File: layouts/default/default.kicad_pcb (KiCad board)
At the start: 2 copper layers, 240 x 47 mm, 129 parts

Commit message: PCB: fix power input orientation and add legends
Route both power cables through the left edge and add durable front and back electrical labels so the assembled dock is unambiguous to power and use.
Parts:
- turned USB1 to 270 degrees
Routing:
- net vdd_cap-power-anode: track 76.1 -> 38.4 mm, vias 10 -> 6
- net DM: track 49.5 -> 15.7 mm, vias 6 -> 0
- net CC2: track 15.5 -> 28.4 mm
- net DP: track 21.5 -> 12.0 mm
- net PG: track 21.2 -> 15.5 mm
- net 9: track 14.2 -> 10.3 mm
- net CC1: track 15.9 -> 16.7 mm, vias 2 -> 0
- net cathode: track 4.63 -> 3.91 mm
- net VBUS: vias 2 -> 0
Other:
- board text added: "12V DC / 5A / CENTER +"
- board text added: "5V OUT / 1A CONT EACH"
- board text added: "INPUT: USB-C PD 12V 36W MAX OR 12V DC 5A CENTER +"
- board text added: "LEDS: RED=PWR BLUE=PD GREEN=CHARGING"
- board text added: "LIGHTBAR DOCK // 8-PORT USB-C CHARGER"
- board text added: "OUTPUT: 5V 1A CONT / PORT (1.5A FUSED)"
- board text added: "PD IN 12V / 36W MAX"
- board text added: "SKG // LIGHTBAR DOCK"
- board text added: "SKG // REV B // 2026"

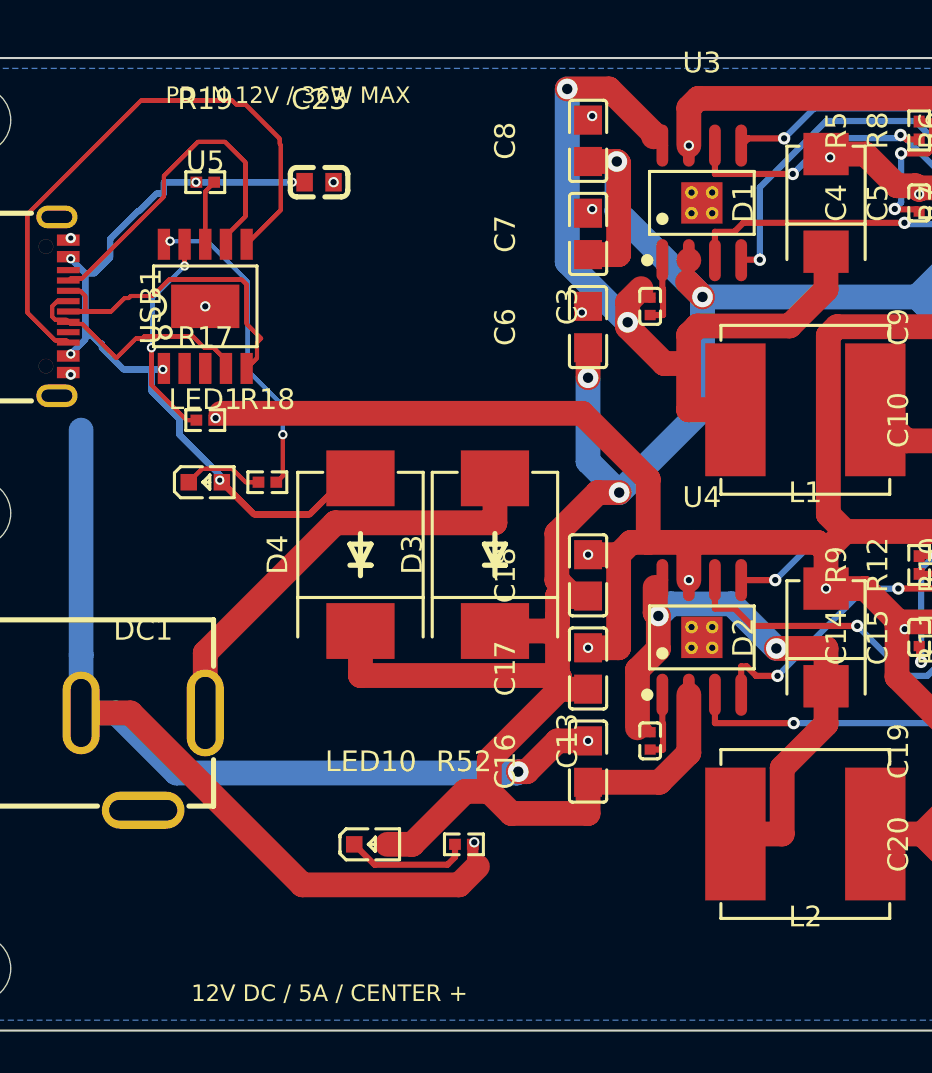
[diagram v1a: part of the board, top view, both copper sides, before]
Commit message: PCB: refresh fabrication outputs and enclosure models
Keep manufacturing and mechanical exports aligned with the corrected power-input geometry and current silkscreen.
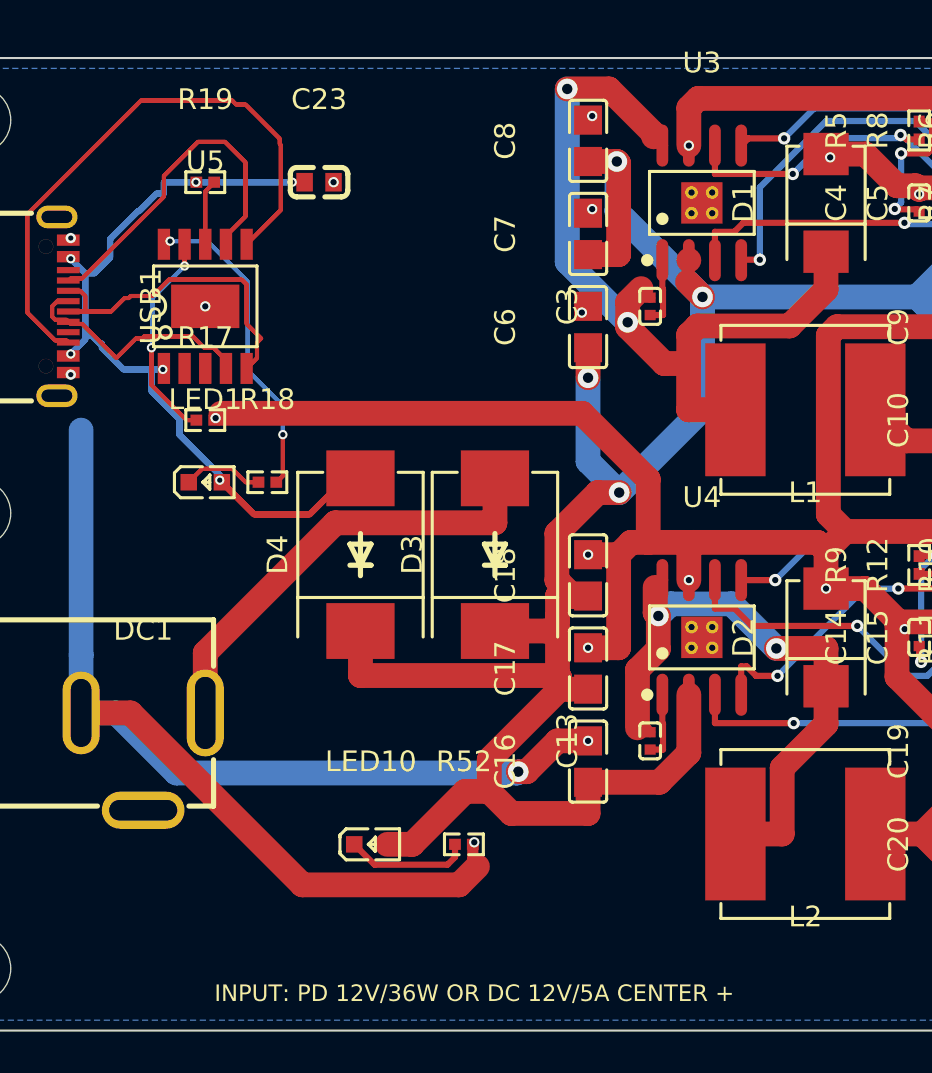
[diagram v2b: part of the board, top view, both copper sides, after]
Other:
- board text added: "INPUT: PD 12V/36W OR DC 12V/5A CENTER +"
- board text removed: "12V DC / 5A / CENTER +"
- board text removed: "PD IN 12V / 36W MAX"
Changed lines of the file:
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@@
 	(footprint "SHOU_HAN_TYPE_C_16PIN_2MD_073:USB-C-SMD_TYPE-C-16PIN-2MD-073"
 		(layer "F.Cu")
-		(at 55 62 270)
+		(at 55 62 -90)
 		(property "Reference" "USB1"
 			(at 0 -6.38 270)
@@
 			)
 			(rotate
-				(xyz 0 0 180)
+				(xyz 0 0 0)
 			)
 		)
@@
 		)
 	)
+	(gr_line
+		(start 50 50)
+		(end 290 50)
+		(stroke
+			(width 0.1)
+			(type default)
+		)
+		(layer "Edge.Cuts")
+	)
+	(gr_line
+		(start 50 97)
+		(end 50 50)
+		(stroke
+			(width 0.1)
+			(type default)
+		)
+		(layer "Edge.Cuts")
+	)
+	(gr_line
+		(start 290 50)
+		(end 290 97)
+		(stroke
+			(width 0.1)
+			(type default)
+		)
+		(layer "Edge.Cuts")
+	)
+	(gr_line
+		(start 290 97)
+		(end 50 97)
+		(stroke
+			(width 0.1)
+			(type default)
+		)
+		(layer "Edge.Cuts")
+	)
+	(gr_text "INPUT: PD 12V/36W OR DC 12V/5A CENTER +"
+		(at 77 95.2 0)
+		(layer "F.SilkS")
+		(effects
+			(font
+				(size 0.8 0.8)
+				(thickness 0.13)
+			)
+		)
+	)
+	(gr_text "5V OUT / 1A CONT EACH"
+		(at 232 95.2 0)
+		(layer "F.SilkS")
+		(effects
+			(font
+				(size 0.8 0.8)
+				(thickness 0.13)
+			)
+		)
+	)
+	(gr_text "SKG // LIGHTBAR DOCK"
+		(at 137 95.2 0)
+		(layer "F.SilkS")
+		(effects
+			(font
+				(size 1.2 1.2)
+				(thickness 0.2)
+			)
+		)
+	)
+	(gr_text "INPUT: USB-C PD 12V 36W MAX OR 12V DC 5A CENTER +"
+		(at 170 71 0)
+		(layer "B.SilkS")
+		(effects
+			(font
+				(size 1 1)
+				(thickness 0.16)
+			)
+			(justify mirror)
+		)
+	)
+	(gr_text "OUTPUT: 5V 1A CONT / PORT (1.5A FUSED)"
+		(at 170 78 0)
+		(layer "B.SilkS")
+		(effects
+			(font
+				(size 1 1)
+				(thickness 0.16)
+			)
+			(justify mirror)
+		)
+	)
+	(gr_text "LEDS: RED=PWR  BLUE=PD  GREEN=CHARGING"
+		(at 170 83 0)
+		(layer "B.SilkS")
+		(effects
+			(font
+				(size 1 1)
+				(thickness 0.16)
+			)
+			(justify mirror)
+		)
+	)
+	(gr_text "SKG // REV B // 2026"
+		(at 170 89 0)
+		(layer "B.SilkS")
+		(effects
+			(font
+				(size 1.5 1.5)
+				(thickness 0.24)
+			)
+			(justify mirror)
+		)
+	)
+	(gr_text "LIGHTBAR DOCK // 8-PORT USB-C CHARGER"
+		(at 170 53.5 0)
+		(layer "B.SilkS")
+		(effects
+			(font
+				(size 1.8 1.8)
+				(thickness 0.28)
+			)
+			(justify mirror)
+		)
+	)
 	(segment
 		(start 160.6684 74.2248)
@@
 	)
 	(embedded_fonts no)
-	(gr_line
-		(start 50 50)
-		(end 290 50)
-		(stroke
-			(width 0.1)
-			(type default)
-		)
-		(layer "Edge.Cuts")
-	)
-	(gr_line
-		(start 290 50)
-		(end 290 97)
-		(stroke
-			(width 0.1)
-			(type default)
-		)
-		(layer "Edge.Cuts")
-	)
-	(gr_line
-		(start 290 97)
-		(end 50 97)
-		(stroke
-			(width 0.1)
-			(type default)
-		)
-		(layer "Edge.Cuts")
-	)
-	(gr_line
-		(start 50 97)
-		(end 50 50)
-		(stroke
-			(width 0.1)
-			(type default)
-		)
-		(layer "Edge.Cuts")
-	)
-	(gr_text "PD IN 12V / 36W MAX"
-		(at 68 51.8)
-		(layer "F.SilkS")
-		(effects
-			(font
-				(size 0.8 0.8)
-				(thickness 0.13)
-			)
-		)
-	)
-	(gr_text "12V DC / 5A / CENTER +"
-		(at 70 95.2)
-		(layer "F.SilkS")
-		(effects
-			(font
-				(size 0.8 0.8)
-				(thickness 0.13)
-			)
-		)
-	)
-	(gr_text "SKG // LIGHTBAR DOCK"
-		(at 137 95.2)
-		(layer "F.SilkS")
-		(effects
-			(font
-				(size 1.2 1.2)
-				(thickness 0.2)
-			)
-		)
-	)
-	(gr_text "5V OUT / 1A CONT EACH"
-		(at 232 95.2)
-		(layer "F.SilkS")
-		(effects
-			(font
-				(size 0.8 0.8)
-				(thickness 0.13)
-			)
-		)
-	)
-	(gr_text "LIGHTBAR DOCK // 8-PORT USB-C CHARGER"
-		(at 170 53.5)
-		(layer "B.SilkS")
-		(effects
-			(font
-				(size 1.8 1.8)
-				(thickness 0.28)
-			)
-			(justify mirror)
-		)
-	)
-	(gr_text "INPUT: USB-C PD 12V 36W MAX OR 12V DC 5A CENTER +"
-		(at 170 71)
-		(layer "B.SilkS")
-		(effects
-			(font
-				(size 1 1)
-				(thickness 0.16)
-			)
-			(justify mirror)
-		)
-	)
-	(gr_text "OUTPUT: 5V 1A CONT / PORT (1.5A FUSED)"
-		(at 170 78)
-		(layer "B.SilkS")
-		(effects
-			(font
-				(size 1 1)
-				(thickness 0.16)
-			)
-			(justify mirror)
-		)
-	)
-	(gr_text "LEDS: RED=PWR  BLUE=PD  GREEN=CHARGING"
-		(at 170 83)
-		(layer "B.SilkS")
-		(effects
-			(font
-				(size 1 1)
-				(thickness 0.16)
-			)
-			(justify mirror)
-		)
-	)
-	(gr_text "SKG // REV B // 2026"
-		(at 170 89)
-		(layer "B.SilkS")
-		(effects
-			(font
-				(size 1.5 1.5)
-				(thickness 0.24)
-			)
-			(justify mirror)
-		)
-	)
 )
